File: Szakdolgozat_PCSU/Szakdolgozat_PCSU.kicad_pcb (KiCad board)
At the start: 4 copper layers, 98 x 98 mm, 64 parts, among them IC1 DRV8244SQDGQRQ1, IC2 TPS54628DDAR, IC3 DRV8244SQDGQRQ1, IC4 LTC4365ITS8-1#TRPBF, J1 MOTOR1_OUT, J2 M1_SPI, J3 M1_CTRL, J4 MOTOR2_OUT, J5 M2_SPI, J6 M2_CTRL, J7 5V_CON, J8 BAT_CON, Q1 STP130N6F7, Q2 STP130N6F7

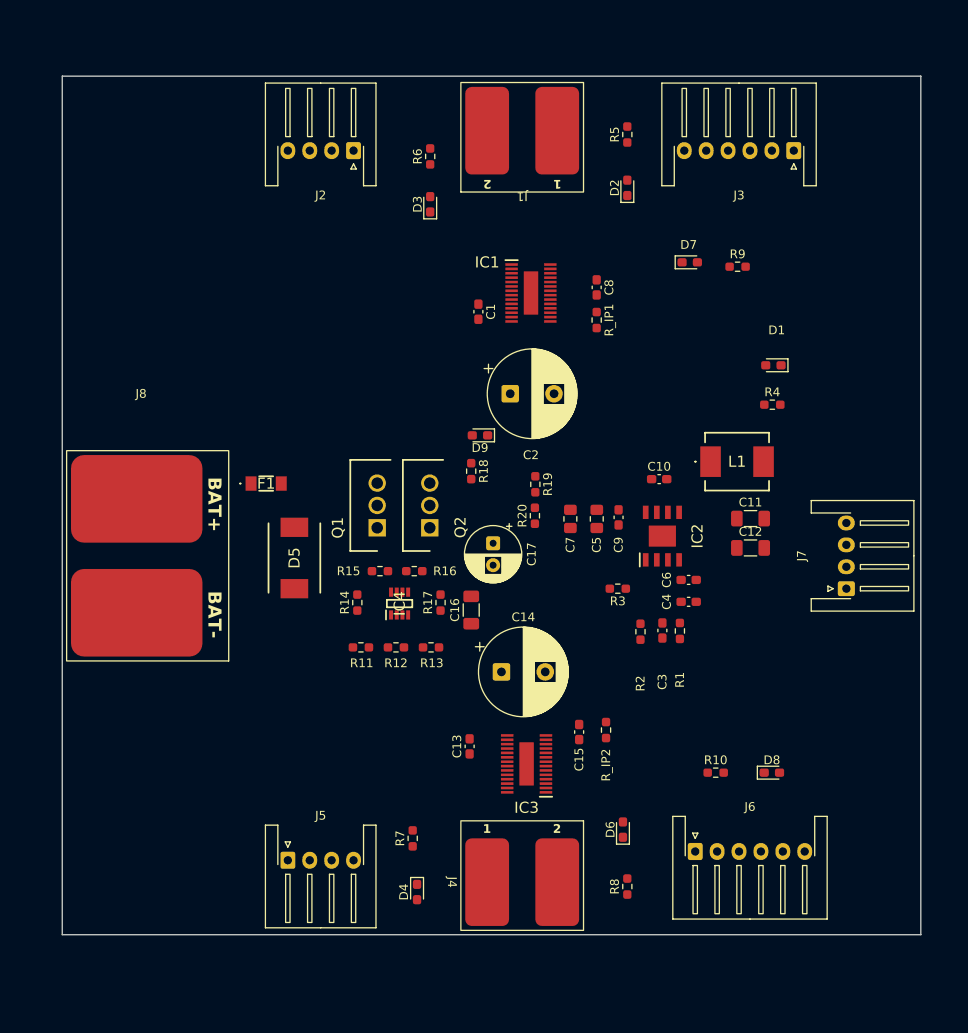
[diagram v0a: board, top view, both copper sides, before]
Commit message: Update PCSU PCB routing, copper pours and vias
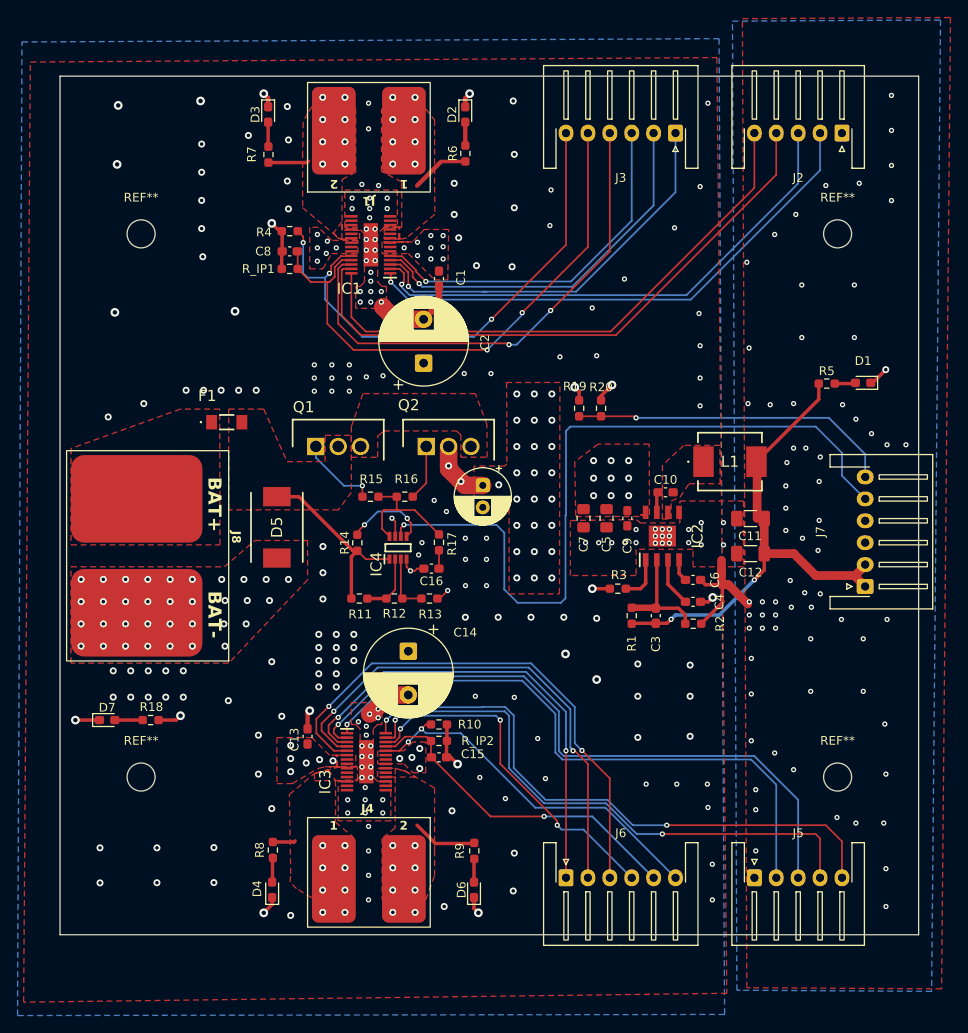
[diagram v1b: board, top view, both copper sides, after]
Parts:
- removed D8: M2_OFF_Y, LED_SMD:LED_0603_1608Metric_Pad1.05x0.95mm_HandSolder
- removed D9: BAT_R, LED_SMD:LED_0603_1608Metric_Pad1.05x0.95mm_HandSolder
- added NT2: NetTie_2, NetTie:Untitled, F.Cu at (123.2, 107.2)
- added REF**: MountingHole_3.2mm_M3, MountingHole:MountingHole_3.2mm_M3, F.Cu at (138.5, 130.0)
- added REF**: MountingHole_3.2mm_M3, MountingHole:MountingHole_3.2mm_M3, F.Cu at (59.0, 68.0)
- added REF**: MountingHole_3.2mm_M3, MountingHole:MountingHole_3.2mm_M3, F.Cu at (138.5, 68.0)
- added REF**: MountingHole_3.2mm_M3, MountingHole:MountingHole_3.2mm_M3, F.Cu at (59.0, 130.0)
- C16: footprint Capacitor_SMD:C_1206_3216Metric_Pad1.33x1.80mm_HandSolder -> Capacitor_SMD:C_0603_1608Metric_Pad1.08x0.95mm_HandSolder
- D7: value M1_OFF_Y -> BAT_R
- J2, J5: footprint Connector_JST:JST_XH_S4B-XH-A-1_1x04_P2.50mm_Horizontal -> Connector_JST:JST_XH_S5B-XH-A-1_1x05_P2.50mm_Horizontal
- J7: footprint Connector_JST:JST_XH_S4B-XH-A-1_1x04_P2.50mm_Horizontal -> Connector_JST:JST_XH_S6B-XH-A-1_1x06_P2.50mm_Horizontal
- R10, R4: value 1k -> 10k
- R5: value 2.7k -> 1k
- R9: value 1k -> 2.7k
- moved D7 84.6 mm to (55.1, 123.5)
- moved R7 79.8 mm to (73.5, 59.0)
- moved R9 73.1 mm to (97.0, 138.4), turned to -90 degrees
- moved R4 58.5 mm to (76.0, 67.7), turned to 180 degrees
- moved J2 55.8 mm to (139.0, 56.5)
- moved J5 53.3 mm to (129.0, 141.5)
- moved R18 46.3 mm to (60.1, 123.5), turned to 180 degrees
- moved R8 40.7 mm to (74.0, 138.3), turned to -90 degrees
- moved R5 36.4 mm to (137.3, 85.1), turned to 0 degrees
- moved R_IP1 35.5 mm to (76.0, 72.0), turned to 180 degrees
- moved C8 35.3 mm to (76.0, 70.0), turned to 180 degrees
- moved R10 32.1 mm to (93.0, 124.0)
- moved D3 21.1 mm to (73.5, 54.4), turned to -90 degrees
- moved D2 20.3 mm to (96.0, 54.4), turned to -90 degrees
- moved R_IP2 19.1 mm to (93.0, 125.9), turned to 0 degrees
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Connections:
- D7 pad 1: GND -> GNDPWR
- F1 pad 2: /12V_FUSE -> /12V_TVS
- IC4 pad 1: /12_TVS -> /12V_TVS
- IC4 pad 4: GND -> GNDPWR
- J2 pad 1: /M1_SCLK -> GND
- J2 pad 2: /~{M1_SCS} -> /M1_SCLK
- J2 pad 3: /M1_SDO -> /~{M1_SCS}
- J2 pad 4: /M1_SDI -> /M1_SDO
- J5 pad 1: /M2_SCLK -> GND
- J5 pad 2: /~{M2_SCS} -> /M2_SCLK
- J5 pad 3: /M2_SDO -> /~{M2_SCS}
- J5 pad 4: /M2_SDI -> /M2_SDO
- J7 pad 2: GND -> /5V
- J7 pad 3: /~{BAT_FAIL} -> GND
- J7 pad 4: /BAT_V -> GND
- Q1 pad 2: /12_TVS -> /12V_TVS
- R10 pad 1: /M2_DRVOFF -> /~{M2_SLEEP}
- R10 pad 2: Net-(D8-A) -> GNDPWR
- R11 pad 1: /12_TVS -> /12V_TVS
- R13 pad 2: GND -> GNDPWR
- R14 pad 1: /12_TVS -> /12V_TVS
- R18 pad 2: Net-(D9-A) -> Net-(D7-A)
- R4 pad 1: /5V -> /~{M1_SLEEP}
- R4 pad 2: Net-(D1-A) -> GNDPWR
- R5 pad 1: /M1_OUT1 -> /5V
- R5 pad 2: Net-(D2-A) -> Net-(D1-A)
- R6 pad 1: /M1_OUT2 -> /M1_OUT1
- R6 pad 2: Net-(D3-A) -> Net-(D2-A)
- R7 pad 1: /M2_OUT1 -> /M1_OUT2
- R7 pad 2: Net-(D4-A) -> Net-(D3-A)
- R8 pad 1: /M2_OUT2 -> /M2_OUT1
- R8 pad 2: Net-(D6-A) -> Net-(D4-A)
- R9 pad 1: /M1_DRVOFF -> /M2_OUT2
- R9 pad 2: Net-(D7-A) -> Net-(D6-A)
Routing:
- net /~{BAT_FAIL}: track 0.00 -> 86.0 mm, vias 0 -> 1
- net /~{M2_SCS}: track 0.00 -> 75.1 mm, vias 0 -> 1
- net /M2_SCLK: track 0.00 -> 70.2 mm, vias 0 -> 1
- net /M1_SDO: track 0.00 -> 69.2 mm
- net /M2_SDI: track 0.00 -> 68.2 mm, vias 0 -> 2
- net /M2_SDO: track 0.00 -> 66.0 mm, vias 0 -> 2
- net /M1_SDI: track 0.00 -> 65.2 mm
- net /M1_IPROPI: track 0.00 -> 64.3 mm, vias 0 -> 2
- net /M2_DRVOFF: track 0.00 -> 61.3 mm, vias 0 -> 2
- net /M1_SCLK: track 0.00 -> 61.2 mm, vias 0 -> 1
- net /~{M1_SLEEP}: track 0.00 -> 61.0 mm, vias 0 -> 3
- net /~{M1_SCS}: track 0.00 -> 60.1 mm, vias 0 -> 1
- net /~{M1_FAULT}: track 0.00 -> 57.9 mm, vias 0 -> 2
- net /M2_EN/IN1: track 0.00 -> 57.7 mm, vias 0 -> 2
- net /5V: track 0.00 -> 56.9 mm, vias 0 -> 2
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- added copper zone on F.Cu, net /12V
- added copper zone on In2.Cu, net /12V
- added copper zone on F.Cu, net /12V_B
- added copper zone on F.Cu, net /12V_TVS
- added copper zone on F.Cu, net /M1_OUT1
- added copper zone on F.Cu, net /M1_OUT2
- added copper zone on F.Cu, net /M2_OUT1
- added copper zone on F.Cu, net /M2_OUT2
- added copper zone on B.Cu, net GND
- added copper zone on F.Cu, net GND
- added copper zone on In1.Cu, net GND
- added copper zone on B.Cu, net GNDPWR
- added copper zone on F.Cu, net GNDPWR
- added copper zone on In1.Cu, net GNDPWR
- added copper zone on F.Cu, net Net-(IC2-SW)
- added copper zone on F.Cu, net Net-(Q1-S)
- removed copper zone on In1.Cu, net /12V
- removed copper zone on In1.Cu, net /5V
- removed copper zone on In2.Cu, net GND
- removed copper zone on In2.Cu, net GNDPWR

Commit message: CU es PCSU Rev A finished + Production Files
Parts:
- added G***: LOGO, LOGO, F.Cu at (119.3, 130.2)
- added G***: LOGO, LOGO, F.Cu at (112.1, 130.2)
- added G***: LOGO, LOGO, F.Cu at (127.4, 130.2)
- moved J7 2.15 mm to (139.5, 108.3)
- moved J5 1.65 mm to (128.9, 139.9)
- moved J2 1.62 mm to (139.0, 58.1)
- moved J3 1.62 mm to (120.0, 58.1)
- moved J6 1.60 mm to (107.5, 139.9)
- renumbered REF** to H1_M3, REF** to H2_M3, REF** to H3_M3, REF** to H4_M3
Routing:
- net /5V: track 56.9 -> 54.7 mm
- net /BAT_V: track 37.0 -> 35.1 mm
- net /M2_SDO: track 66.0 -> 64.3 mm
- net /M2_SCLK: track 70.2 -> 68.5 mm
- net /~{M2_SCS}: track 75.1 -> 73.4 mm
- net /M2_SDI: track 68.2 -> 66.5 mm
- net /M1_SDI: track 65.2 -> 63.6 mm
- net /M1_EN/IN1: track 43.6 -> 42.0 mm
- net /M1_DRVOFF: track 41.7 -> 40.1 mm
- net /~{M1_SLEEP}: track 61.0 -> 59.4 mm
- net /M1_SCLK: track 61.2 -> 59.6 mm
- net /~{M1_SCS}: track 60.1 -> 58.5 mm
- net /~{M1_FAULT}: track 57.9 -> 56.3 mm
- net /M1_SDO: track 69.2 -> 67.6 mm
- net /M1_PH/IN2: track 46.6 -> 45.0 mm
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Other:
- board text added: "Katona Attila Zoltán VZOLU7 POWER & MOTOR CONTROL UNIT 2026 | REV A"
